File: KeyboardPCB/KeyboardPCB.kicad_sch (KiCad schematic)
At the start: 2 parts, among them P1 USB_C_Plug, P2 USB_C_Plug

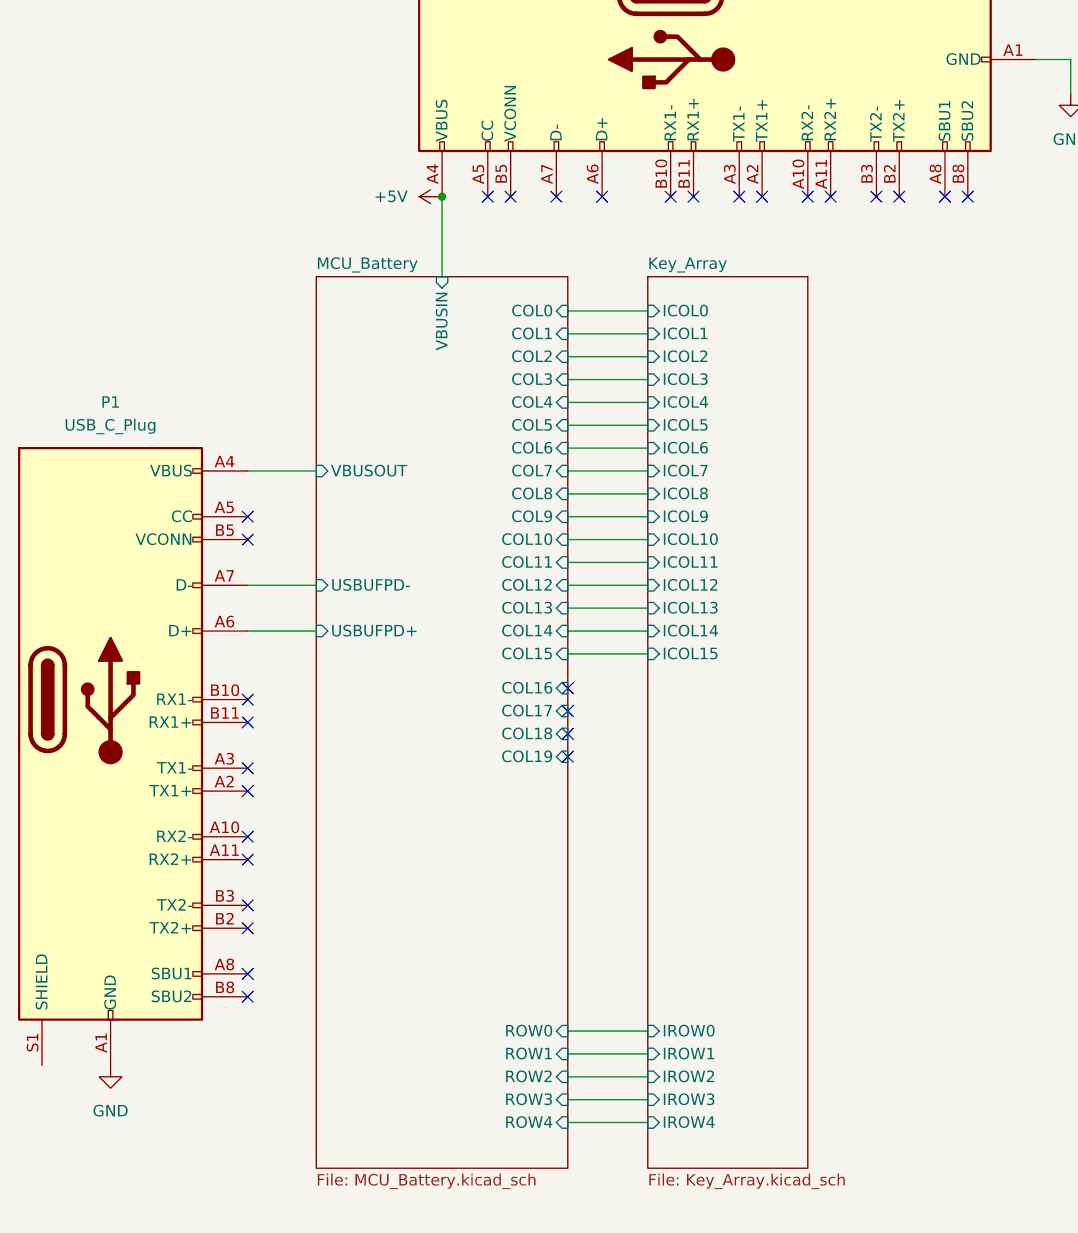
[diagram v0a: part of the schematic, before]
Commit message: Added some Capacitors
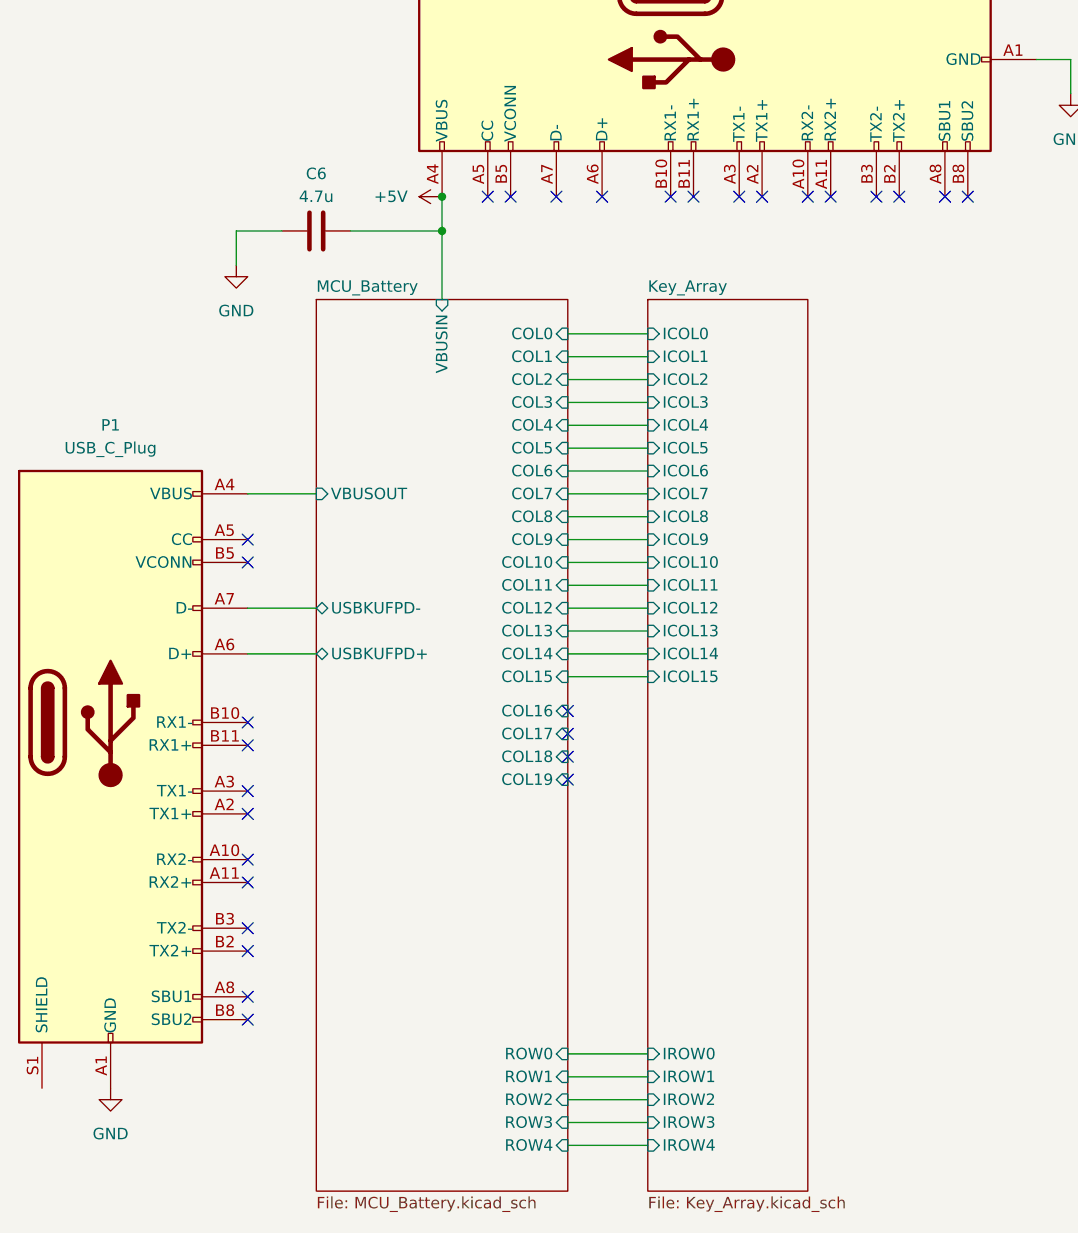
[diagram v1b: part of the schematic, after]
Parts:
- added C6: 4.7u, symbol Device:C
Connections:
- net +5V: now also C6.1
- net GND: now also C6.2
- net MCU_Battery/USBUFPD+ renamed MCU_Battery/USBKUFPD+
- net MCU_Battery/USBUFPD- renamed MCU_Battery/USBKUFPD-
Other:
- sheet MCU_Battery ports: added USBKUFPD+, USBKUFPD-; removed USBUFPD+, USBUFPD-
- moved on the sheet: P1

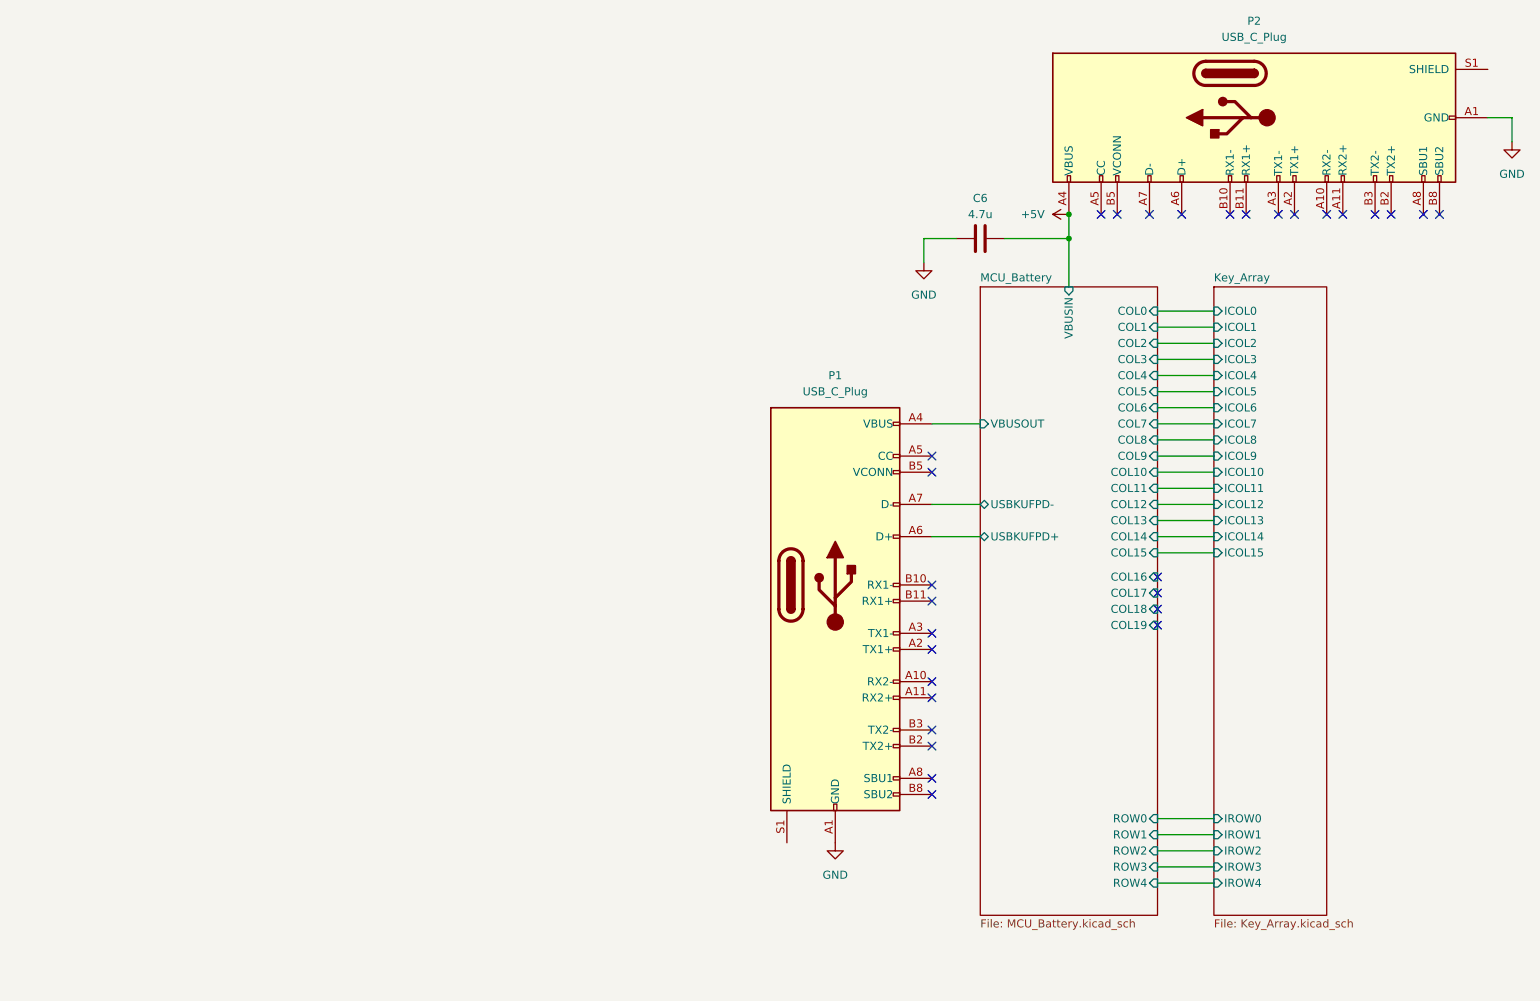
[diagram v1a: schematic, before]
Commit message: added footprints and changed symbols
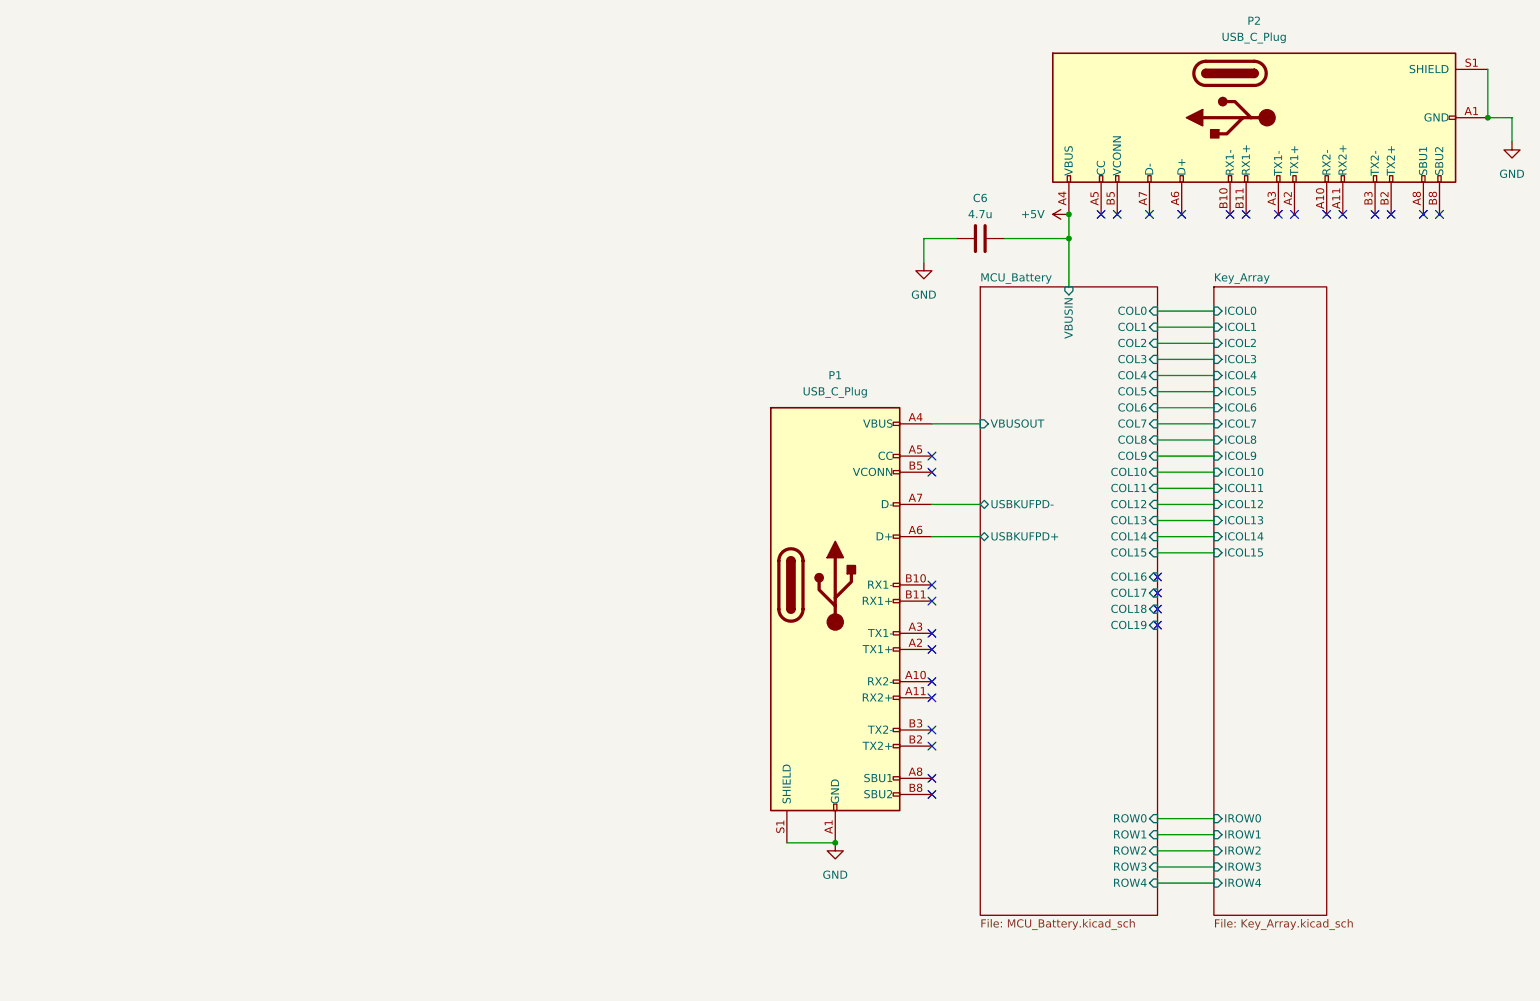
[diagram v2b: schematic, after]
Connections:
- net GND: now also P1.S1 (SHIELD), P2.S1 (SHIELD)
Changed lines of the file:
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@@
 (kicad_sch (version 20230121) (generator eeschema)
   (paper "A4")
+  (junction (at 271.78 34.29) (diameter 0) (color 0 0 0 0)
+  )
   (junction (at 205.74 53.34) (diameter 0) (color 0 0 0 0)
+  )
+  (junction (at 168.91 148.59) (diameter 0) (color 0 0 0 0)
   )
   (junction (at 205.74 49.53) (diameter 0) (color 0 0 0 0)
@@
     (stroke (width 0) (type default))
   )
+  (wire (pts (xy 271.78 26.67) (xy 271.78 34.29))
+    (stroke (width 0) (type default))
+  )
   (wire (pts (xy 187.96 53.34) (xy 182.88 53.34))
     (stroke (width 0) (type default))
@@
     (stroke (width 0) (type default))
   )
+  (wire (pts (xy 161.29 148.59) (xy 168.91 148.59))
+    (stroke (width 0) (type default))
+  )

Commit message: Added Symbols and placed them
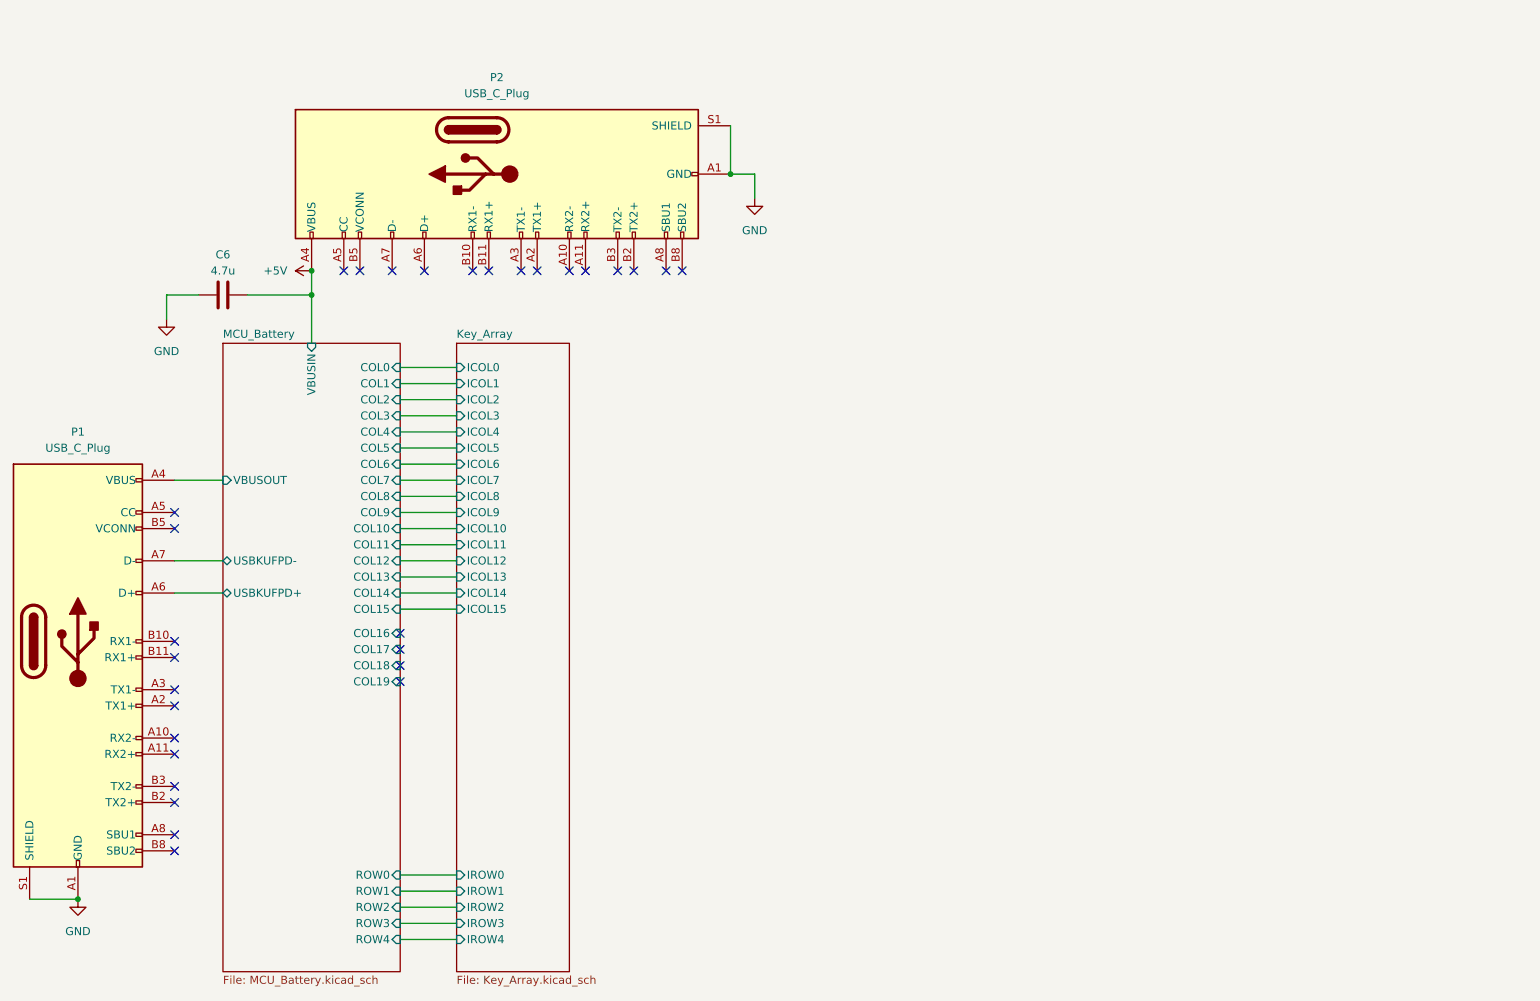
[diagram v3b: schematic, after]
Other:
- moved on the sheet: C6, P1, P2

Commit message: changed several components
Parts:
- removed C6: 4.7u, symbol Device:C
- added C5: UMK107ABJ105KA8T, keyboard_syms:CAPC1608X95N, symbol keyboard_syms:UMK107ABJ105KA8T
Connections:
- net +5V: now also C5.2
- net GND: now also C5.1

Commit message: made changes to the board
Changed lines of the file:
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@@
       (effects (font (size 1.27 1.27)) (justify right))
     )
-    (pin "VBUSOUT" input (at 74.93 91.44 180)
+    (pin "VBUSOUT" output (at 74.93 91.44 180)
       (effects (font (size 1.27 1.27)) (justify left))
     )

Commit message: Schematic Filled out
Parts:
- P1, P2: footprint (none) -> Connector_USB:USB_C_Receptacle_Amphenol_12401548E4-2A
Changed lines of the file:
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@@
       (effects (font (size 1.27 1.27)))
     )
-    (property "Footprint" "" (at 111.76 46.99 0)
+    (property "Footprint" "Connector_USB:USB_C_Receptacle_Amphenol_12401548E4-2A" (at 111.76 46.99 0)
       (effects (font (size 1.27 1.27)) hide)
     )
@@
       (effects (font (size 1.27 1.27)))
     )
-    (property "Footprint" "" (at 53.34 116.84 0)
+    (property "Footprint" "Connector_USB:USB_C_Receptacle_Amphenol_12401548E4-2A" (at 53.34 116.84 0)
       (effects (font (size 1.27 1.27)) hide)
     )

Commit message: Finalised schematic, progress on board layout
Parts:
- renumbered C5 to C1
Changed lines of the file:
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@@
   (symbol (lib_id "keyboard_syms:UMK107ABJ105KA8T") (at 68.58 62.23 0) (unit 1)
     (in_bom yes) (on_board yes) (dnp no) (fields_autoplaced)
-    (property "Reference" "C5" (at 68.58 54.61 0)
+    (property "Reference" "C1" (at 68.58 54.61 0)
       (effects (font (size 1.27 1.27)))
     )
@@
       (project "KeyboardPCB"
         (path "/0ddec2b6-b97f-44d3-913e-9f8ffaa22885"
-          (reference "C5") (unit 1)
+          (reference "C1") (unit 1)
         )
       )
